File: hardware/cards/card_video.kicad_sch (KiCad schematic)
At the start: 41 parts, among them J1 HDMI_A, J2 VGA HD15, M1 Core2350B (8MB PSRAM), U2 74LVC245A, U3 74LVC245A, U4 74LVC245A, U5 74LVC245A, U6 74LVC245A, U7 74LVC245A

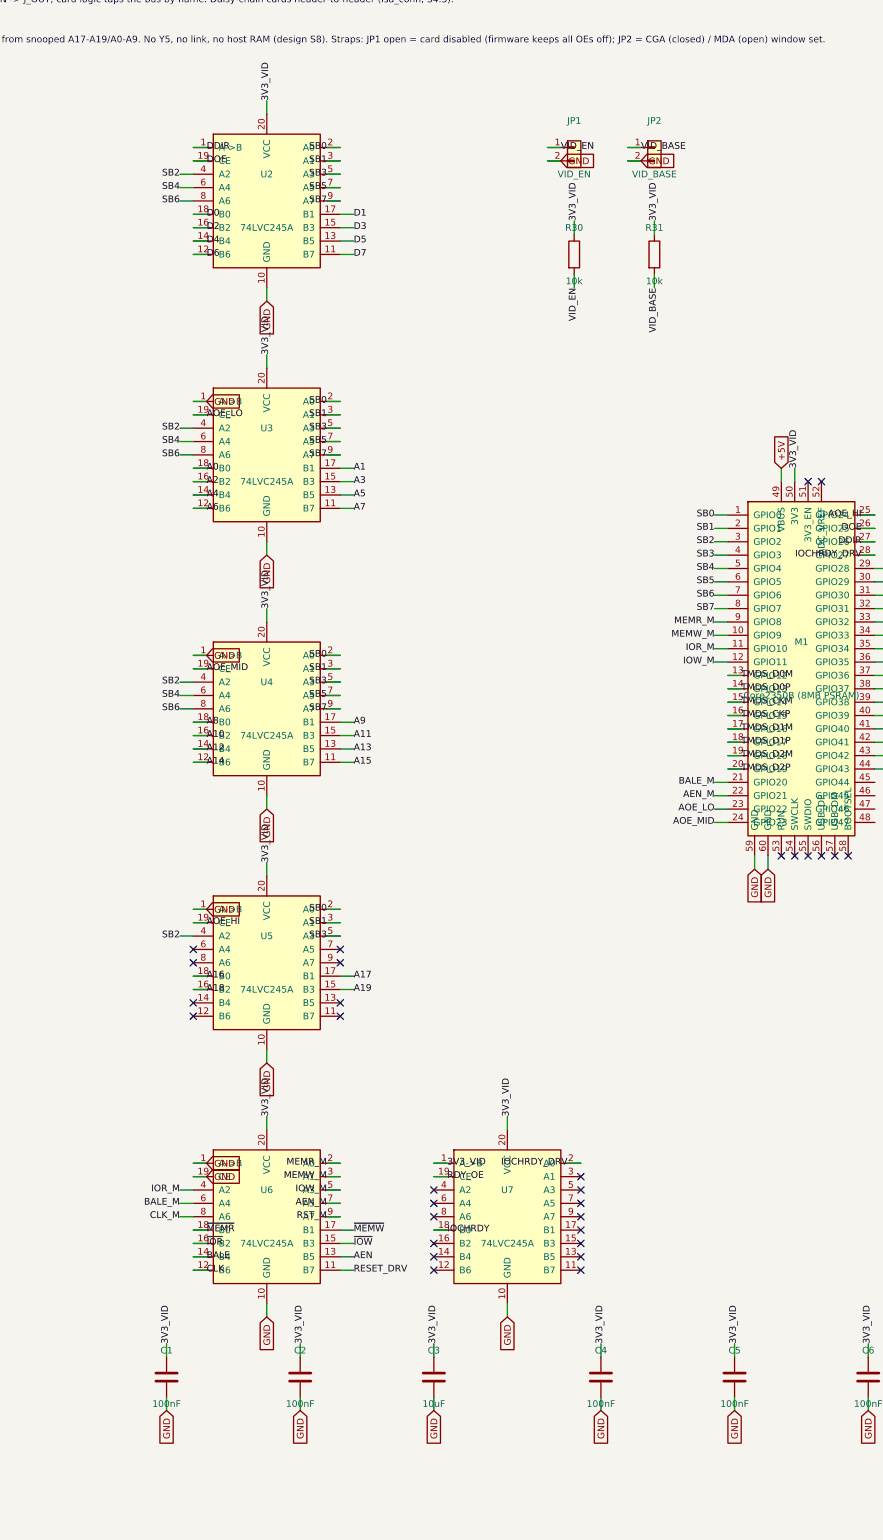
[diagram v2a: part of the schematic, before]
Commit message: Core2350B sites: VBUS diode-OR + Hi-Z shifter parking
The Waveshare Core2350B has NO diode between its on-module USB connector
and its VBUS pin (vendor schematic, hardware/Core2350B.pdf) -- with both
module sites tied straight to +5V, plugging a PC in for firmware flashing
would back-power the whole board (board off) or parallel two hard 5V
supplies (board on).

- D1 (SS34) per site, Pico-style: +5V -> anode, module VBUS -> cathode
  (nets VBUS_MCU / VBUS_VID). USB flashing powers only the module; a
  running board never back-drives the PC port. The ME6217 LDO has ample
  headroom at ~4.7 V in.
- Hi-Z parking so a BOOTSEL/pre-init MCU (all GPIO Hi-Z) never drives the
  5 V bus through the shifters: bus_mcu R16-R18 (DATADIR B->A sense --
  U2's enable is hard-grounded; M_TC low; HLDA low, defining U6's
  direction when the V20 side is unpowered); video R32-R37 (DOE/AOE_*/
  RDY_OE to 3V3_VID = active-low enables parked off, DDIR low). Before
  this, those controls floated whenever firmware wasn't driving them.

Doc 12 gains a "module-USB flashing is safe" bullet; decisions logged in
questions-bus_mcu.md / questions-video.md. card_video inherits the diode
and pulls automatically.

Verified: motherboard + cards rebuild with zero structural ERC; netlist
shows VBUS_MCU/VBUS_VID = {module VBUS, D cathode} only, and each parking
net = {module GPIO, resistor, shifter pin} (HLDA additionally spans its
12-node handoff group with R218).

Co-Authored-By: Claude Fable 5 <noreply@anthropic.com>
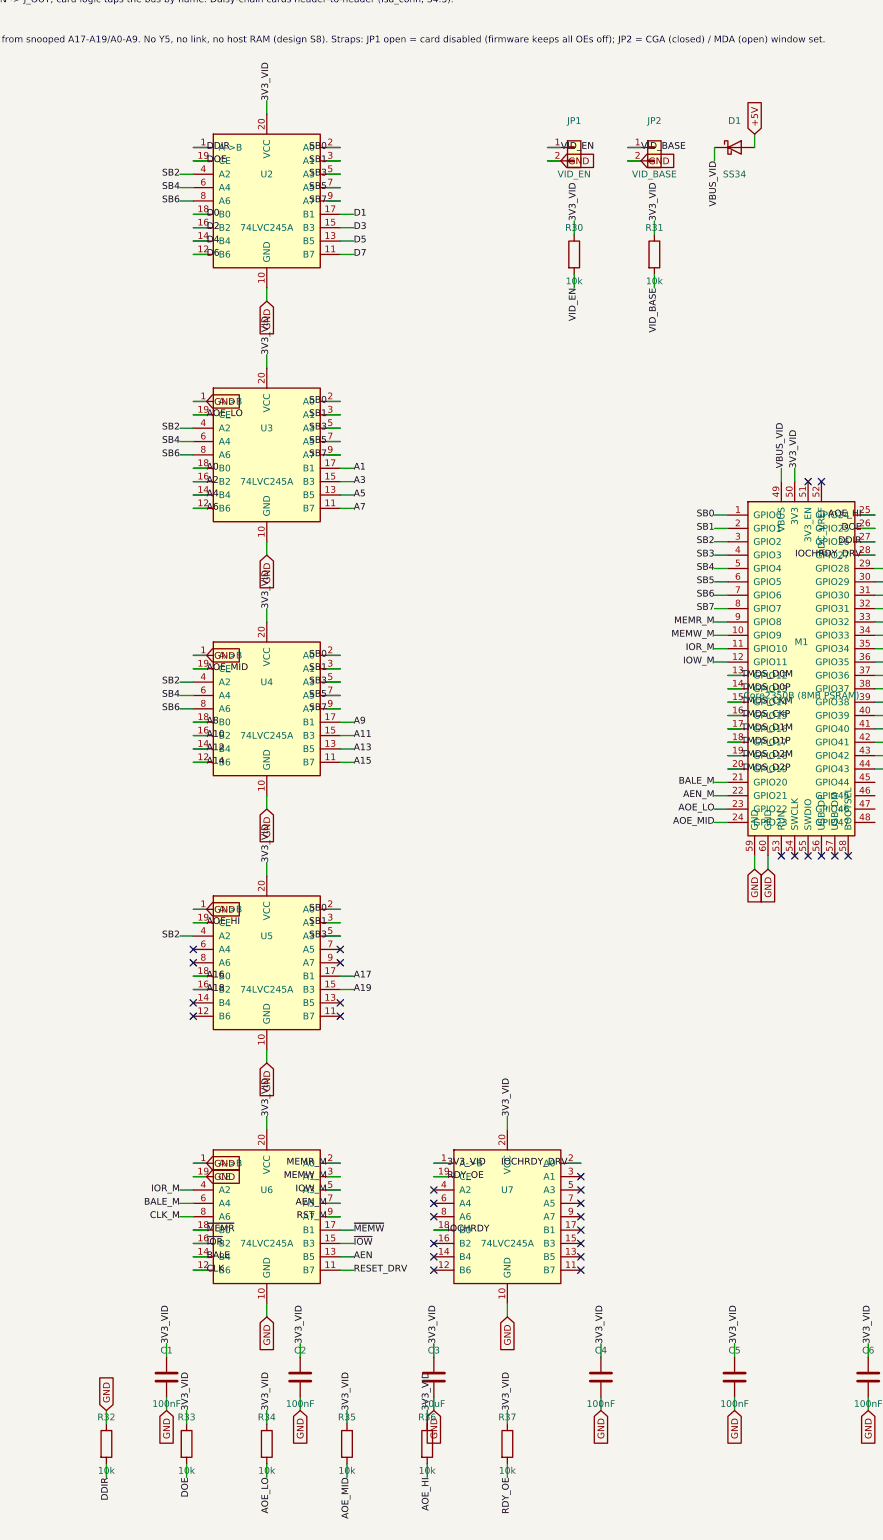
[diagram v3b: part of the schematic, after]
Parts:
- removed R10, R11, R12: 270, symbol Device:R
- removed R20, R23: 2k, symbol Device:R
- removed R21: 1k, symbol Device:R
- removed R22: 510, symbol Device:R
- added J2: VGA HD15, symbol Connector_Generic:Conn_01x15
- added JP1: VID_EN, symbol Connector_Generic:Conn_01x02
- added JP2: VID_BASE, symbol Connector_Generic:Conn_01x02
- added R15, R16, R17: 270, symbol Device:R
- added R27: 510, symbol Device:R
- added R28, R29: 100, symbol Device:R
- added R30, R31, R36, R37: 10k, symbol Device:R
- added U2: 74LVC245A, symbol mini-xt:74LVC245A
- C2: renamed from C3; value 10uF -> 100nF; LCSC Part Num C15850 -> C14663
- C3: renamed from C4; value 100nF -> 10uF; LCSC Part Num C14663 -> C15850
- C7: renamed from JP1; value VID_EN -> 100nF; symbol Connector_Generic:Conn_01x02 -> Device:C; LCSC Part Num C2337 -> C14663
- D1: renamed from C1; value 100nF -> SS34; symbol Device:C -> Device:D_Schottky; LCSC Part Num C14663 -> (none)
- R20: renamed from R27; value 510 -> 2k; LCSC Part Num C23193 -> C22975
- R21: renamed from R28; value 100 -> 1k; LCSC Part Num C22775 -> C21190
- R22: renamed from R29; value 100 -> 510; LCSC Part Num C22775 -> C23193
- R23: renamed from J2; value VGA HD15 -> 2k; symbol Connector_Generic:Conn_01x15 -> Device:R; LCSC Part Num (none) -> C22975
- R32: renamed from JP2; value VID_BASE -> 10k; symbol Connector_Generic:Conn_01x02 -> Device:R; LCSC Part Num C2337 -> C25804
- R35: renamed from U2; value 74LVC245A -> 10k; symbol mini-xt:74LVC245A -> Device:R; LCSC Part Num C6082 -> C25804
- renumbered C2 to C1, C5 to C4, C6 to C5, C7 to C6, R15 to R10, R16 to R11, R17 to R12, R30 to R33, R31 to R34
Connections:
- net +5V: now also D1.2 (A); no longer M1.49 (VBUS)
- net 3V3_VID: now also C7.1, R35.1, R30.1, R31.1, R36.1, R37.1, U2.20 (VCC); no longer D1.1, R35.20 (VCC)
- net AOE_HI: now also R36.2
- net AOE_LO: now also R34.2
- net AOE_MID: now also R35.2
- net D0: now also U2.18 (B0); no longer R35.18 (B0)
- net D1: now also U2.17 (B1); no longer R35.17 (B1)
- net D2: now also U2.16 (B2); no longer R35.16 (B2)
- net D3: now also U2.15 (B3); no longer R35.15 (B3)
- net D4: now also U2.14 (B4); no longer R35.14 (B4)
- net D5: now also U2.13 (B5); no longer R35.13 (B5)
- net D6: now also U2.12 (B6); no longer R35.12 (B6)
- net D7: now also U2.11 (B7); no longer R35.11 (B7)
- net DDIR: now also R32.2, U2.1 (A->B); no longer R35.1 (A->B)
- net DOE: now also R33.2, U2.19 (CE); no longer R35.19 (CE)
- net GND: now also R32.1, J2.10 (Pin_10), J2.5 (Pin_5), J2.6 (Pin_6), J2.7 (Pin_7), J2.8 (Pin_8), JP1.2 (Pin_2), JP2.2 (Pin_2), U2.10 (GND); no longer D1.2, R23.10 (Pin_10), R23.5 (Pin_5), R23.6 (Pin_6), R23.7 (Pin_7), R23.8 (Pin_8), R32.2 (Pin_2), R35.10 (GND)
- net HDMI_CKM: now also R17.2; no longer R12.2
- net HDMI_CKP: now also R16.2; no longer R11.2
- net HDMI_D0M: now also R15.2; no longer R10.2
- net HDMI_D1P: now also R12.2
- net HDMI_D2M: now also R11.2
- net HDMI_D2P: now also R10.2
- net HSYNC: now also R28.1; no longer R21.1
- net HSYNC_J: now also J2.13 (Pin_13), R28.2; no longer R21.2, R23.13 (Pin_13)
- net RDY_OE: now also R37.2
- net SB0: now also U2.2 (A0); no longer R35.2 (A0)
- net SB1: now also U2.3 (A1); no longer R35.3 (A1)
- net SB2: now also U2.4 (A2); no longer R35.4 (A2)
- net SB3: now also U2.5 (A3); no longer R35.5 (A3)
- net SB4: now also U2.6 (A4); no longer R35.6 (A4)
- net SB5: now also U2.7 (A5); no longer R35.7 (A5)
- net SB6: now also U2.8 (A6); no longer R35.8 (A6)
- net SB7: now also U2.9 (A7); no longer R35.9 (A7)
- net TMDS_CKM: now also R17.1; no longer R12.1
- net TMDS_CKP: now also R16.1; no longer R11.1
- net TMDS_D0M: now also R15.1; no longer R10.1
- net TMDS_D1P: now also R12.1
- net TMDS_D2M: now also R11.1
- net TMDS_D2P: now also R10.1
- net VB1: now also R27.1; no longer R20.1
- net VG0: now also R23.1
- net VGA_B: now also J2.3 (Pin_3), R27.2; no longer R20.2, R23.3 (Pin_3)
- net VGA_G: now also J2.2 (Pin_2)
- net VGA_R: now also R20.2, R21.2, R22.2, J2.1 (Pin_1); no longer R23.1 (Pin_1)
- net VID_BASE: now also JP2.1 (Pin_1), R31.2; no longer R32.1 (Pin_1), R34.2
- net VID_EN: now also JP1.1 (Pin_1), R30.2; no longer C7.1 (Pin_1), R33.2
- net VR0: now also R20.1
- net VR1: now also R21.1
- net VR2: now also R22.1
- net VSYNC: now also R29.1; no longer R22.1
- net VSYNC_J: now also J2.14 (Pin_14), R29.2; no longer R22.2, R23.14 (Pin_14)
- new net VBUS_VID: D1.1 (K), M1.49 (VBUS)
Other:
- moved on the sheet: C1, C2, C3, C4, C5, C6, R10, R11, R12, R20, R21, R22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

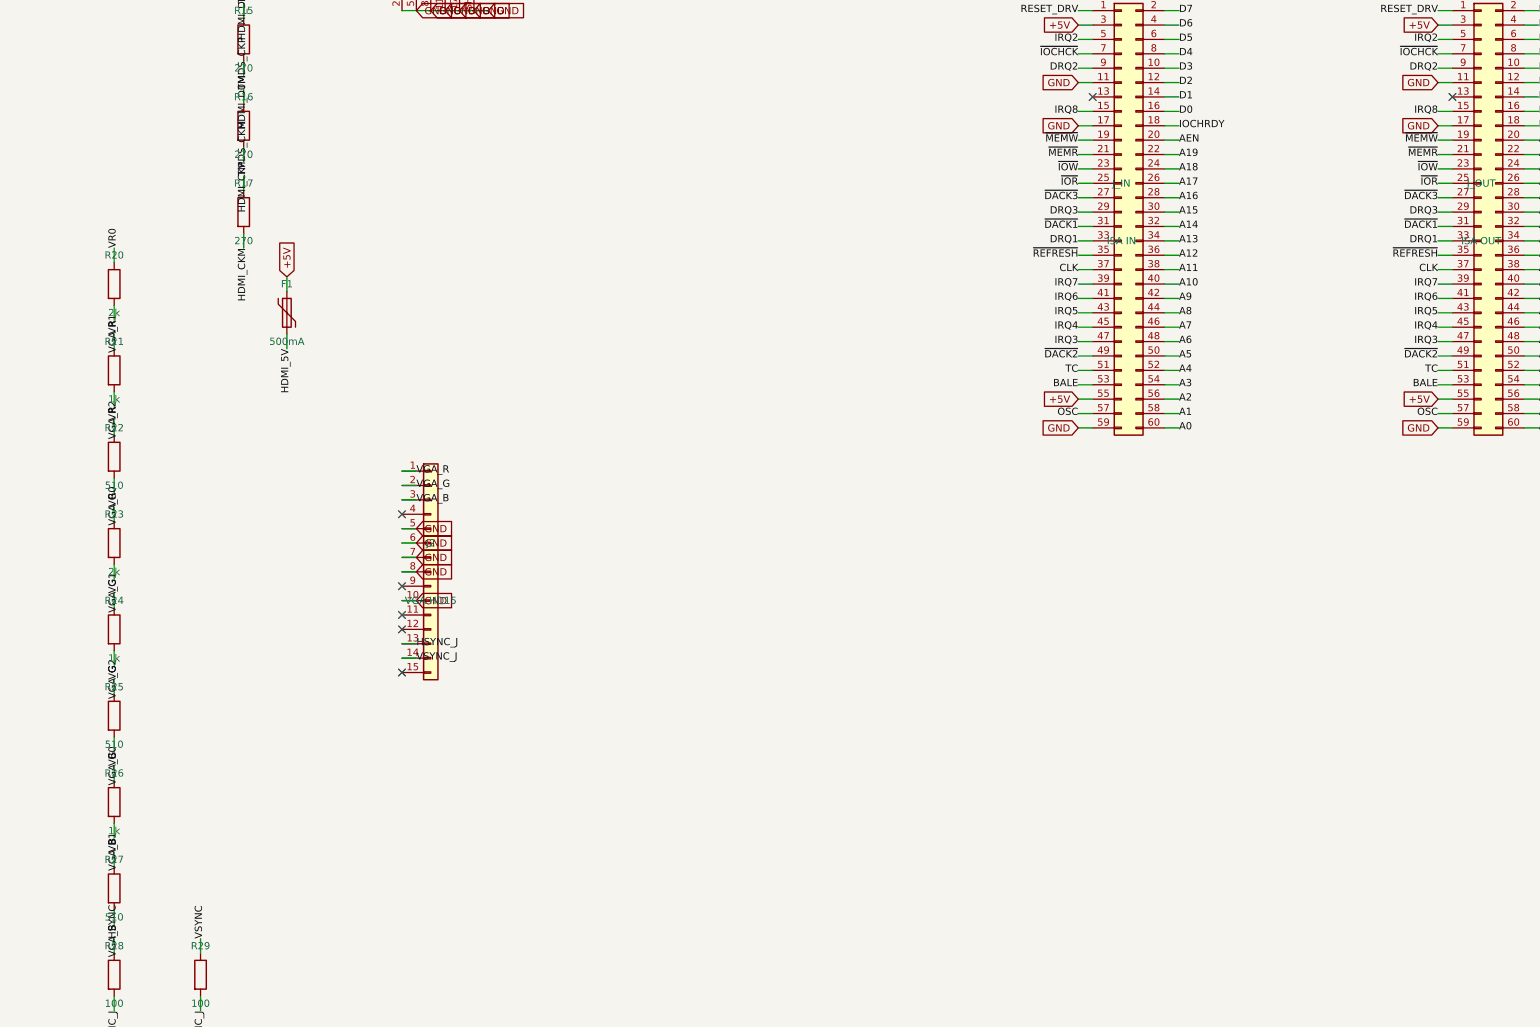
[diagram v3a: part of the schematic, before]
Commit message: Design-review fixes: reset parking, IRQ8 off the header, analog cleanups
Netlist-wide review sweep. IRQ8 leaves the 60-pin ISA header (pin 15 is a
second GND return; the on-board RTC owns IRQ8 exclusively, so its push-pull
drive is now correct by construction). Bus MCU Hi-Z parking completed:
~CPURESET pulled low (V20 held in reset while the MCU is unprogrammed),
~DACK1/~REFRESH parked deasserted, DRQ1 idled low. Supervisor 12 MHz crystal
damping R actually in series now (was parallel-to-nothing), plus a second
USBLC6 so both prog-port SW2 positions are ESD-protected. Audio: 0.5x PG
summing (MCP6002 headroom), 100k LINE bleed, unit B parked as a follower --
and the SUM stub moved off pin 5's row, where wiring unit B would have
silently merged SUM into VREF. CH224K VDD fed through 1k per the WCH ref
design. VGA blue ladder rescaled 1k/510 -> 820/470 (was ~12% blue-deficient).
Spare CMOS gate inputs grounded uniformly (cpu_core/rtc/storage); UART_RXD
pulled up (SIN idles at mark with JP1 open); dead pins/parts dropped
(com_port CLK, parallel RESET_DRV, storage R3). Bus CLK fixed at 7.16 MHz
logged as a decision. New passives mapped to JLC basic parts in parts.py.

Co-Authored-By: Claude Fable 5 <noreply@anthropic.com>
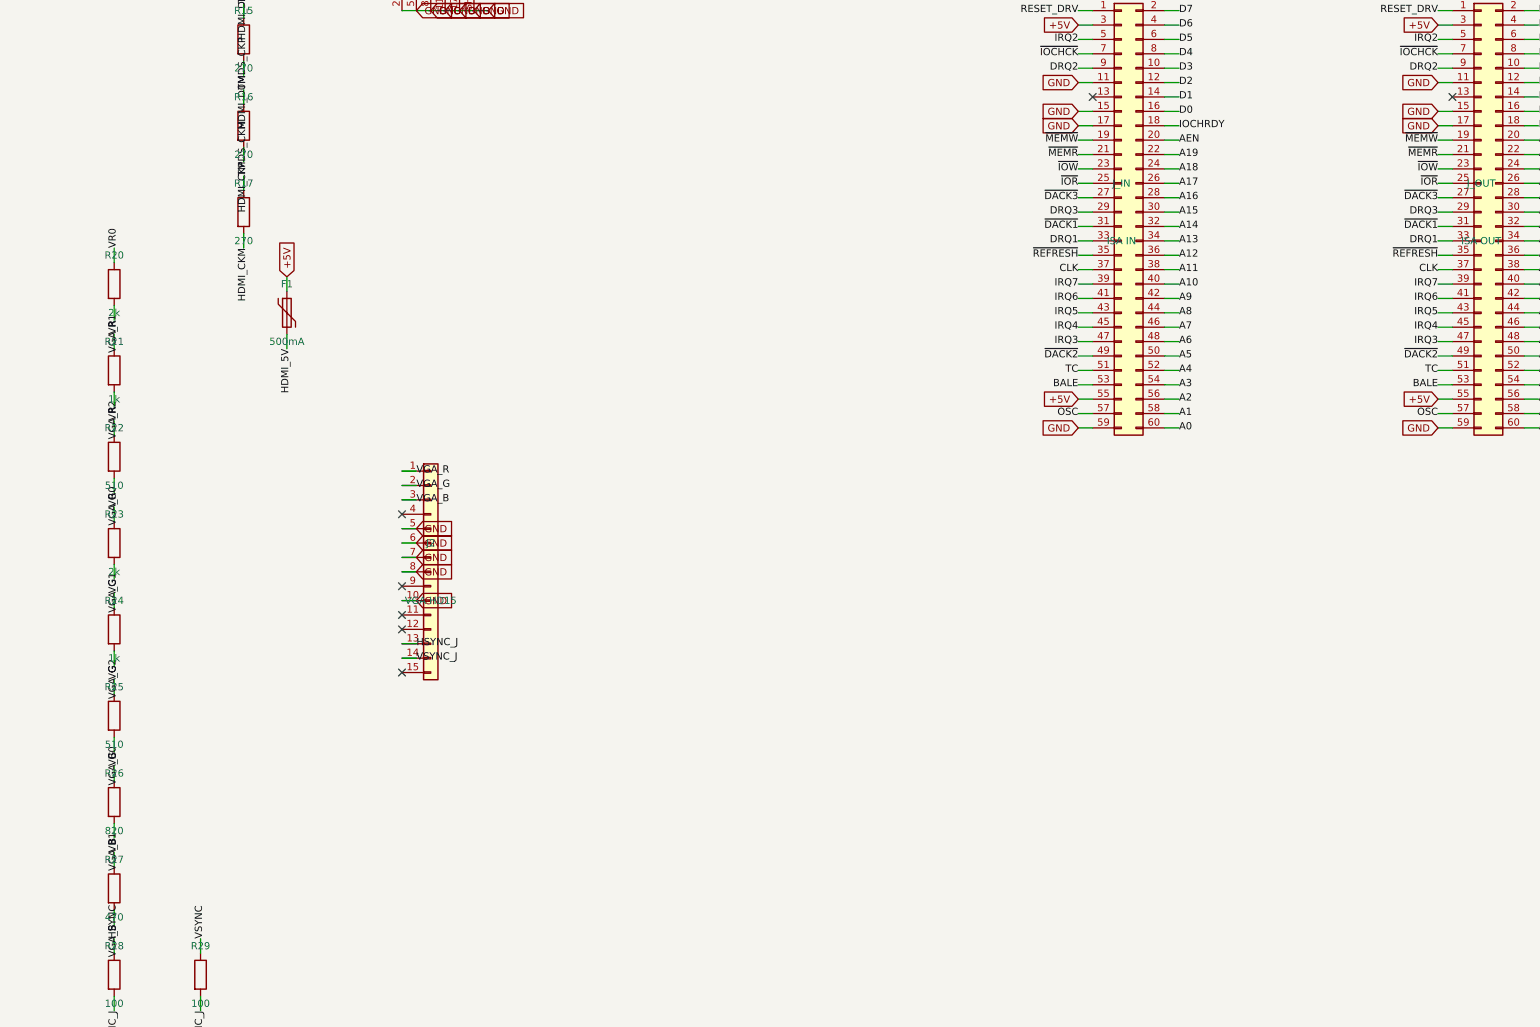
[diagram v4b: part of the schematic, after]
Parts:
- R26: value 1k -> 820; LCSC Part Num C21190 -> C23253
- R27: value 510 -> 470; LCSC Part Num C23193 -> C23179
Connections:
- net IRQ8 is gone; now on net GND: J_IN.15 (Pin_15), J_OUT.15 (Pin_15)
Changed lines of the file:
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@@
 		)
 	)
-	(label "IRQ8"
+	(global_label "GND"
+		(shape input)
 		(at 436.88 134.62 180)
 		(effects
@@
 		)
 	)
-	(label "IRQ8"
+	(global_label "GND"
+		(shape input)
 		(at 500.38 134.62 180)
 		(effects
@@
 			)
 		)
-		(property "Value" "1k"
+		(property "Value" "820"
 			(at 266.7 261.62 0)
 			(effects
@@
 			)
 		)
-		(property "LCSC Part Num" "C21190"
+		(property "LCSC Part Num" "C23253"
 			(at 266.7 256.54 0)
 			(effects
@@
 			)
 		)
-		(property "Value" "510"
+		(property "Value" "470"
 			(at 266.7 276.86 0)
 			(effects
@@
 			)
 		)
-		(property "LCSC Part Num" "C23193"
+		(property "LCSC Part Num" "C23179"
 			(at 266.7 271.78 0)
 			(effects
